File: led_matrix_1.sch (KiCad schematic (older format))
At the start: 64 parts

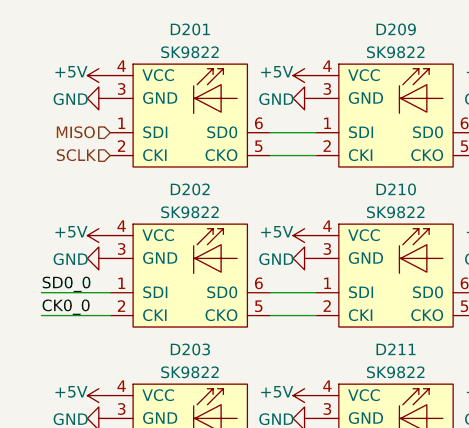
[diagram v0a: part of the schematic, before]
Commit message: update Schema
-pwr flag eingefügt
-3.3V Analog Netzleibel eingefügt
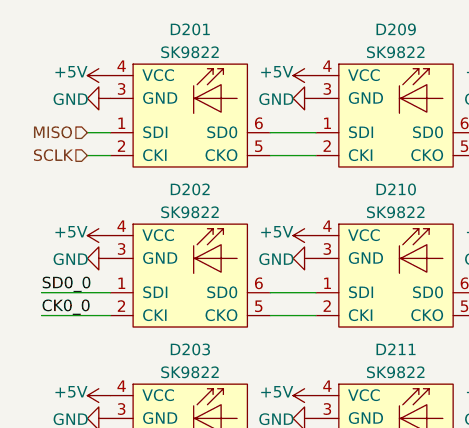
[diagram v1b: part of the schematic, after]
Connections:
- wire segments 140 -> 142
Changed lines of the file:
@@
 Wire Wire Line
 	8700 2550 8950 2550
-Text HLabel 1700 1150 0    50   Input ~ 0
+Text HLabel 1600 1150 0    50   Input ~ 0
 MISO
-Text HLabel 1700 1250 0    50   Input ~ 0
+Text HLabel 1600 1250 0    50   Input ~ 0
 SCLK
 NoConn ~ 8700 6050
@@
 	1    0    0    -1
 $EndComp
+Wire Wire Line
+	1700 1150 1600 1150
+Wire Wire Line
+	1700 1250 1600 1250
 $EndSCHEMATC

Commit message: update schema
-MISO to MOSI
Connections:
- net labels added: MOSI
- net labels removed: MISO
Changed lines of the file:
@@
 Wire Wire Line
 	8700 2550 8950 2550
-Text HLabel 1600 1150 0    50   Input ~ 0
-MISO
 Text HLabel 1600 1250 0    50   Input ~ 0
 SCLK
@@
 Wire Wire Line
 	1700 1250 1600 1250
+Text HLabel 1600 1150 0    50   Input ~ 0
+MOSI
 $EndSCHEMATC

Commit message: Update Schema
Footprint
Netlist
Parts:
- D201, D202, D203, D204, D205, D206, D207, D208, D209, D210, D211, D212, D213, D214, D215, D216, D217, D218, D219, D220, D221, D222, D223, D224, D225, D226, D227, D228, D229, D230, D231, D232, D233, D234, D235, D236, D237, D238, D239, D240, D241, D242, D243, D244, D245, D246, D247, D248, D249, D250, D251, D252, D253, D254, D255, D256, D257, D258, D259, D260, D261, D262, D263, D264: footprint (none) -> myFoodprints:SK9822
